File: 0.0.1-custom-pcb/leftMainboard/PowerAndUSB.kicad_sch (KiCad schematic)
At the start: 31 parts, among them J1 USB-C USB2 receptacle (footpr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, J2 3-pin LiPo / NTC 1.25mm (esti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, Q2 P-channel MOSFET (guess), Q3 P-channel MOSFET (guess), SW1 Latching DPDT power push swit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, U1 Boost controller MSOP8 (unide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, U2 TP4056-42-ESOP8, U3 PRTR5V0U2X

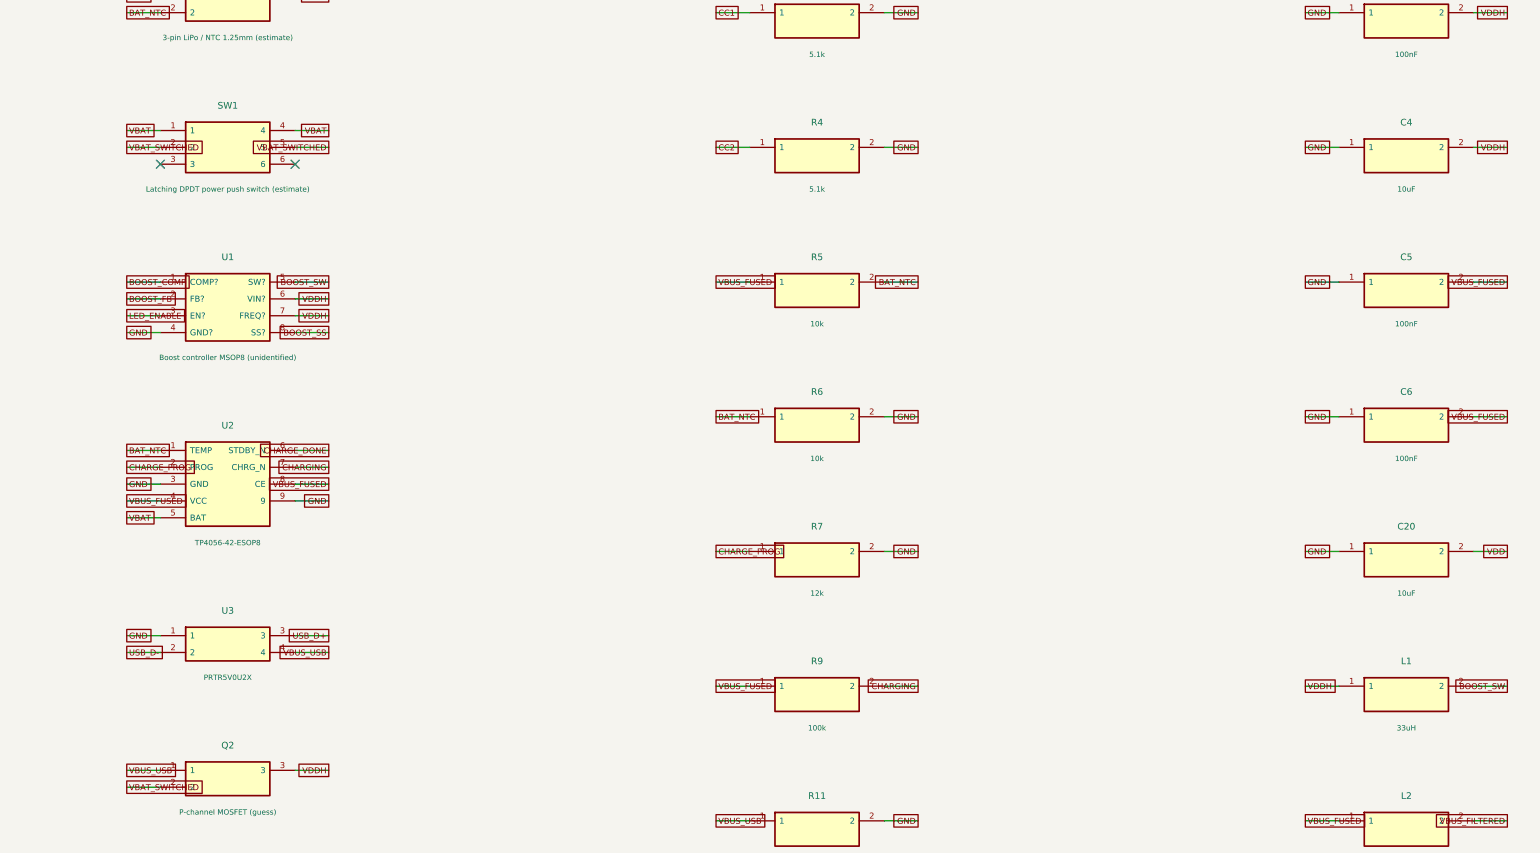
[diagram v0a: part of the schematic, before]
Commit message: get correct main switch
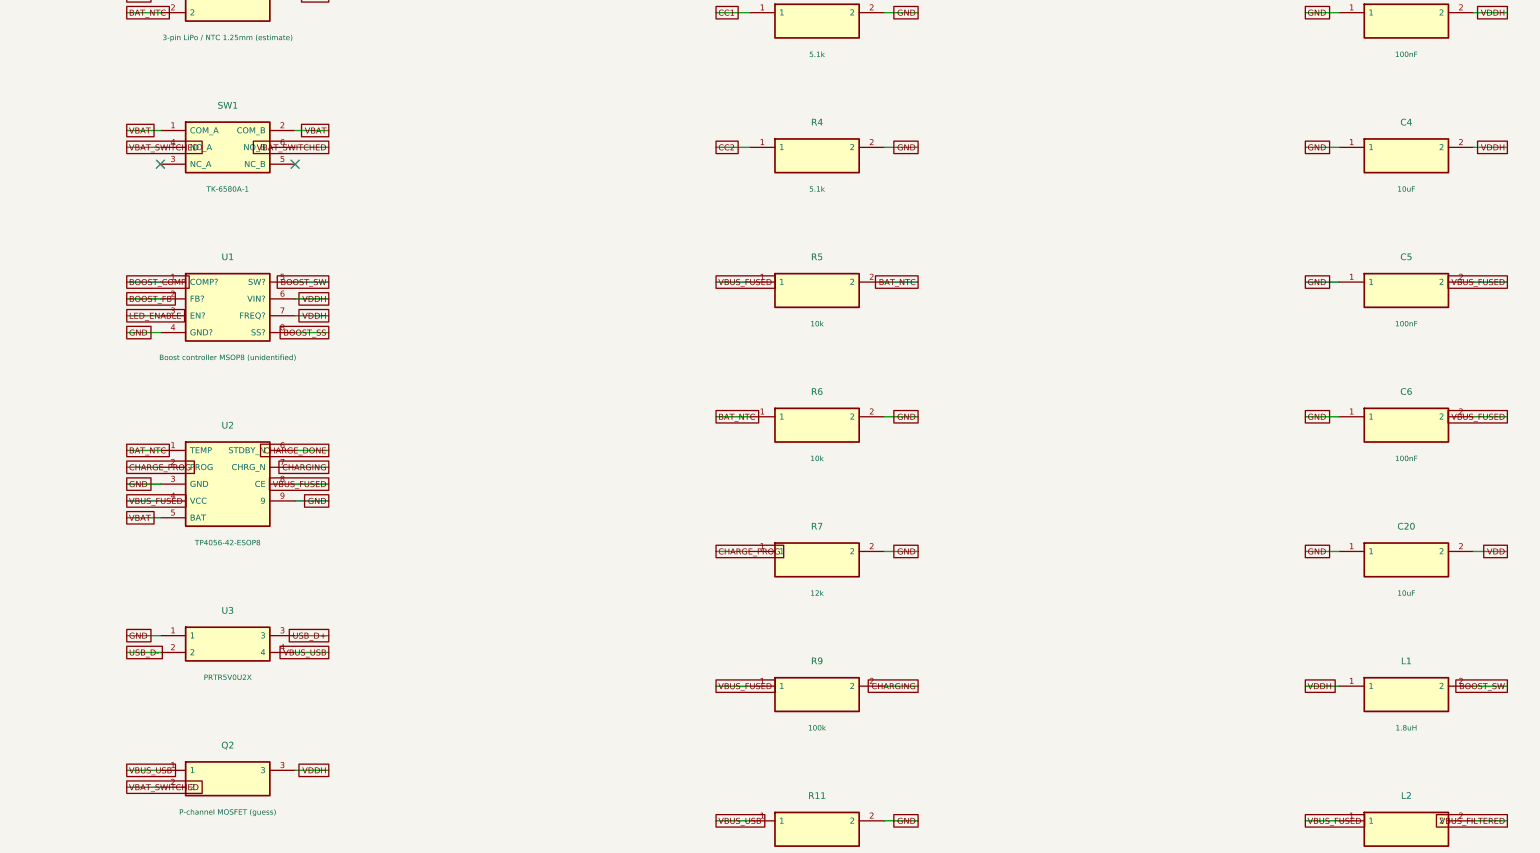
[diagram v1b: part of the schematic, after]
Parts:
- L1: value 33uH -> 1.8uH; footprint Reconstruction:L1_Inductor_6x6mm_PhotoEstimate -> Reconstruction:L_XRCD54_5.8x5.2mm_C5339378; symbol Reconstruction:L1_L1_Inductor_6x6mm_PhotoEstimate -> Reconstruction:L_XRCD54_1R8M_C5339378; Candidate part (none) -> XRCD54-1R8M; Confidence High (33uH marking) -> User-selected replacement; original part unconfirmed; Evidence L1 marked 330; L2/L3 values and exact function inferred -> C5339378 selected by user; supersedes photo-estimated 33uH; LCSC Part (none) -> C5339378; MPN (none) -> XRCD54-1R8M; Manufacturer (none) -> XR
- SW1: value Latching DPDT power push switch (estimate) -> TK-6580A-1; footprint Reconstruction:PowerSwitch_DPDT_LH_PhotoEstimate -> Reconstruction:SW_TK6580A1_C528770; symbol Reconstruction:SW1_PowerSwitch_DPDT_LH_PhotoEstimate -> Reconstruction:SW_TK6580A1_C528770; Candidate part PS-22F family, verify dimensional drawing -> TK-6580A-1; Confidence Low -> User-selected replacement; original part unconfirmed; Evidence Push actuator + six contacts + mechanical lugs visible; exa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 -> User-selected replacement; footprint and models from JLCEDA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; LCSC Part (none) -> C528770; MPN (none) -> TK-6580A-1; Manufacturer (none) -> Yuandi
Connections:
- net VBAT: now also SW1.2 (COM_B); no longer SW1.4
- net VBAT_SWITCHED: now also SW1.4 (NO_A), SW1.6 (NO_B); no longer SW1.2, SW1.5
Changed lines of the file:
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@@
 (no_connect (at 66.04 110.49)
 )
-(symbol (lib_id "Reconstruction:SW1_PowerSwitch_DPDT_LH_PhotoEstimate")
-(at 55.88 107.94999999999999 0)
-(unit 1)
-(exclude_from_sim no)
-(in_bom yes)
-(on_board yes)
-(dnp no)
-(property "Reference" "SW1" (at 55.88 101.63999999999999 0)
-(effects (font (size 1.0 1.0))))
-(property "Value" "Latching DPDT power push switch (estimate)" (at 55.88 114.25999999999999 0)
-(effects (font (size 0.8 0.8))))
-(property "Footprint" "Reconstruction:PowerSwitch_DPDT_LH_PhotoEstimate" (at 55.88 107.94999999999999 0)
-(effects (font (size 1.0 1.0))
-(hide yes)))
-(property "Datasheet" "" (at 55.88 107.94999999999999 0)
-(effects (font (size 1.0 1.0))
-(hide yes)))
-(property "Confidence" "Low" (at 55.88 107.94999999999999 0)
-(effects (font (size 1.0 1.0))
-(hide yes)))
-(property "Evidence" "Push actuator + six contacts + mechanical lugs visible; exact switch/terminal function unverified" (at 55.88 107.94999999999999 0)
-(effects (font (size 1.0 1.0))
-(hide yes)))
-(property "Candidate part" "PS-22F family, verify dimensional drawing" (at 55.88 107.94999999999999 0)
-(effects (font (size 1.0 1.0))
-(hide yes)))
-(pin "1")
-(pin "2")
-(pin "3")
-(pin "4")
-(pin "5")
-(pin "6")
-(instances (project "leftMainboard" (path "/eac6e0a1-0901-4c4d-b0b4-c941afc6d33b/3d4a4145-dfbf-4d53-839d-da2f670b524e" (reference "SW1")
-(unit 1)))))
+(symbol (lib_id "Reconstruction:SW_TK6580A1_C528770") (at 55.88 107.94999999999999 0) (unit 1) (exclude_from_sim no) (in_bom yes) (on_board yes) (dnp no) (property "Reference" "SW1" (at 55.88 101.63999999999999 0) (effects (font (size 1.0 1.0)))) (property "Value" "TK-6580A-1" (at 55.88 114.25999999999999 0) (effects (font (size 0.8 0.8)))) (property "Footprint" "Reconstruction:SW_TK6580A1_C528770" (at 55.88 107.94999999999999 0) (effects (font (size 1.0 1.0)) (hide yes))) (property "Datasheet" "https://wmsc.lcsc.com/wmsc/upload/file/pdf/v2/lcsc/2304140030_Yuandi-TK-6580A-1_C528770.pdf" (at 55.88 107.94999999999999 0) (effects (font (size 1.0 1.0)) (hide yes))) (property "Confidence" "User-selected replacement; original part unconfirmed" (at 55.88 107.94999999999999 0) (effects (font (size 1.0 1.0)) (hide yes))) (property "Evidence" "User-selected replacement; footprint and models from JLCEDA/EasyEDA Official Library; pin function checked against manufacturer drawing" (at 55.88 107.94999999999999 0) (effects (font (size 1.0 1.0)) (hide yes))) (property "Candidate part" "TK-6580A-1" (at 55.88 107.94999999999999 0) (effects (font (size 1.0 1.0)) (hide yes))) (pin "1") (pin "4") (pin "3") (pin "2") (pin "6") (pin "5") (instances (project "leftMainboard" (path "/eac6e0a1-0901-4c4d-b0b4-c941afc6d33b/3d4a4145-dfbf-4d53-839d-da2f670b524e" (reference "SW1") (unit 1)))) (property "LCSC Part" "C528770" (at 55.88 107.94999999999999 0) (effects (font (size 1.0 1.0)) (hide yes))) (property "Manufacturer" "Yuandi" (at 55.88 107.94999999999999 0) (effects (font (size 1.0 1.0)) (hide yes))) (property "MPN" "TK-6580A-1" (at 55.88 107.94999999999999 0) (effects (font (size 1.0 1.0)) (hide yes))))
 (wire (pts (xy 45.72 128.27)
 (xy 40.64 128.27))
@@
 (effects (font (size 1.0 1.0))
 (hide yes))))
-(symbol (lib_id "Reconstruction:L1_L1_Inductor_6x6mm_PhotoEstimate")
-(at 233.68 190.49999999999994 0)
-(unit 1)
-(exclude_from_sim no)
-(in_bom yes)
-(on_board yes)
-(dnp no)
-(property "Reference" "L1" (at 233.68 185.45999999999995 0)
-(effects (font (size 1.0 1.0))))
-(property "Value" "33uH" (at 233.68 195.53999999999994 0)
-(effects (font (size 0.8 0.8))))
-(property "Footprint" "Reconstruction:L1_Inductor_6x6mm_PhotoEstimate" (at 233.68 190.49999999999994 0)
-(effects (font (size 1.0 1.0))
-(hide yes)))
-(property "Datasheet" "" (at 233.68 190.49999999999994 0)
-(effects (font (size 1.0 1.0))
-(hide yes)))
-(property "Confidence" "High (33uH marking)" (at 233.68 190.49999999999994 0)
-(effects (font (size 1.0 1.0))
-(hide yes)))
-(property "Evidence" "L1 marked 330; L2/L3 values and exact function inferred" (at 233.68 190.49999999999994 0)
-(effects (font (size 1.0 1.0))
-(hide yes)))
-(property "Candidate part" "" (at 233.68 190.49999999999994 0)
-(effects (font (size 1.0 1.0))
-(hide yes)))
-(pin "1")
-(pin "2")
-(instances (project "leftMainboard" (path "/eac6e0a1-0901-4c4d-b0b4-c941afc6d33b/3d4a4145-dfbf-4d53-839d-da2f670b524e" (reference "L1")
-(unit 1)))))
+(symbol (lib_id "Reconstruction:L_XRCD54_1R8M_C5339378") (at 233.68 190.49999999999994 0) (unit 1) (exclude_from_sim no) (in_bom yes) (on_board yes) (dnp no) (property "Reference" "L1" (at 233.68 185.45999999999995 0) (effects (font (size 1.0 1.0)))) (property "Value" "1.8uH" (at 233.68 195.53999999999994 0) (effects (font (size 0.8 0.8)))) (property "Footprint" "Reconstruction:L_XRCD54_5.8x5.2mm_C5339378" (at 233.68 190.49999999999994 0) (effects (font (size 1.0 1.0)) (hide yes))) (property "Datasheet" "https://wmsc.lcsc.com/wmsc/upload/file/pdf/v2/lcsc/2212281609_XR-XRCD54-1R8M_C5339378.pdf" (at 233.68 190.49999999999994 0) (effects (font (size 1.0 1.0)) (hide yes))) (property "Confidence" "User-selected replacement; original part unconfirmed" (at 233.68 190.49999999999994 0) (effects (font (size 1.0 1.0)) (hide yes))) (property "Evidence" "C5339378 selected by user; supersedes photo-estimated 33uH" (at 233.68 190.49999999999994 0) (effects (font (size 1.0 1.0)) (hide yes))) (property "Candidate part" "XRCD54-1R8M" (at 233.68 190.49999999999994 0) (effects (font (size 1.0 1.0)) (hide yes))) (pin "1") (pin "2") (instances (project "leftMainboard" (path "/eac6e0a1-0901-4c4d-b0b4-c941afc6d33b/3d4a4145-dfbf-4d53-839d-da2f670b524e" (reference "L1") (unit 1)))) (property "LCSC Part" "C5339378" (at 233.68 190.49999999999994 0) (effects (font (size 1 1)) (hide yes))) (property "Manufacturer" "XR" (at 233.68 190.49999999999994 0) (effects (font (size 1 1)) (hide yes))) (property "MPN" "XRCD54-1R8M" (at 233.68 190.49999999999994 0) (effects (font (size 1 1)) (hide yes))))
 (wire (pts (xy 223.52 209.55)
 (xy 218.44 209.55))

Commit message: update a couple components to be correct
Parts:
- J2: value 3-pin LiPo / NTC 1.25mm (estimate) -> 53398-0371; footprint Reconstruction:Battery_3pin_1.25mm_PhotoEstimate -> Reconstruction:J_Molex_53398_0371_C293633; symbol Reconstruction:J2_Battery_3pin_1.25mm_PhotoEstimate -> Reconstruction:J_Molex_53398_0371_C293633; Candidate part JST GH / Molex PicoBlade 1.25mm family -> 53398-0371; Confidence Low (MPN and polarity) -> User-selected replacement; original part unconfirmed; Evidence 3-pin housing and three wires visible; pitch estimated from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 -> User-selected C293633 replacement; Molex PicoBlade 53398-03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; LCSC Part (none) -> C293633; MPN (none) -> 53398-0371; Manufacturer (none) -> Molex
- U1: value Boost controller MSOP8 (unidentified) -> SY7088DGC; footprint Reconstruction:U1_MSOP-8_3x3mm_P0.65mm -> Reconstruction:DFN8_SY7088DGC_2x3mm_C178240; symbol Reconstruction:U1_U1_MSOP-8_3x3mm_P0.65mm -> Reconstruction:U_SY7088DGC_C178240; Candidate part TPS61085-class MSOP8 boost; NOT confirmed pin-compatible -> SY7088DGC; Confidence Low -> High: marking and body size match; selected replacement; Evidence Marking looks MXCEA/M1CEA, unreadable ID. Guessed functiona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 -> User-reported VTGEA marking and approximately 2.1x3 mm body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; LCSC Part (none) -> C178240; MPN (none) -> SY7088DGC; Manufacturer (none) -> Silergy
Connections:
- net BOOST_COMP is gone; now on net BOOST_SW: U1.1 (LX)
- net BOOST_SS is gone; now on net VDD: U1.8 (OUT)
- net BOOST_FB: now also U1.5 (FB); no longer U1.2 (FB?)
- net BOOST_SW: now also U1.2 (LX); no longer U1.5 (SW?)
- net GND: now also J2.3 (GND), U1.9 (PGND); no longer J2.1
- net VBAT: now also J2.1 (VBAT); no longer J2.3
- net VDD: now also U1.7 (OUT)
- net VDDH: no longer U1.7 (FREQ?)

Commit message: update more of left main
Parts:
- F1: value 500mA resettable fuse (guess) -> MF-NSMF150-2; Confidence Medium (function), Low (rating) -> User selected; Evidence Gold B-marked rectangular part is likely PPTC USB protection -> Selected by user from the 8 marking and measured 3.4 x 1.8 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; LCSC (none) -> C89655; LCSC Part (none) -> C89655; MPN (none) -> MF-NSMF150-2; Manufacturer (none) -> Bourns
- Q3: value P-channel MOSFET (guess) -> BSS138 N-channel; Candidate part AO3401A / SI2301 family -> BSS138; Confidence Low -> Medium; Evidence 3-lead packages; faint SS/G marking; polarity and part numb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 -> User measured body about 3x1.3 mm, marking SS; diode-mode d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; LCSC (none) -> C7420339
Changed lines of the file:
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@@
 (property "Reference" "Q3" (at 55.88 218.47999999999996 0)
 (effects (font (size 1.0 1.0))))
-(property "Value" "P-channel MOSFET (guess)" (at 55.88 228.55999999999995 0)
+(property "Value" "BSS138 N-channel" (at 55.88 228.55999999999995 0)
 (effects (font (size 0.8 0.8))))
 (property "Footprint" "Reconstruction:Q3_SOT-23" (at 55.88 223.51999999999995 0)
 (effects (font (size 1.0 1.0))
 (hide yes)))
-(property "Datasheet" "" (at 55.88 223.51999999999995 0)
-(effects (font (size 1.0 1.0))
-(hide yes)))
-(property "Confidence" "Low" (at 55.88 223.51999999999995 0)
-(effects (font (size 1.0 1.0))
-(hide yes)))
-(property "Evidence" "3-lead packages; faint SS/G marking; polarity and part number unconfirmed" (at 55.88 223.51999999999995 0)
-(effects (font (size 1.0 1.0))
-(hide yes)))
-(property "Candidate part" "AO3401A / SI2301 family" (at 55.88 223.51999999999995 0)
+(property "Datasheet" "https://www.lcsc.com/datasheet/C7420339.pdf" (at 55.88 223.51999999999995 0)
+(effects (font (size 1.0 1.0))
+(hide yes)))
+(property "LCSC" "C7420339" (at 55.88 223.51999999999995 0)
+(effects (font (size 1.0 1.0))
+(hide yes)))
+(property "Confidence" "Medium" (at 55.88 223.51999999999995 0)
+(effects (font (size 1.0 1.0))
+(hide yes)))
+(property "Evidence" "User measured body about 3x1.3 mm, marking SS; diode-mode display 440 (about 0.440 V), pins 1/2 shorted, red 2 black 3; supports N-channel; reverse reading and isolated-device test not reported; exact MPN unconfirmed" (at 55.88 223.51999999999995 0)
+(effects (font (size 1.0 1.0))
+(hide yes)))
+(property "Candidate part" "BSS138" (at 55.88 223.51999999999995 0)
 (effects (font (size 1.0 1.0))
 (hide yes)))
@@
 (property "Reference" "F1" (at 322.58000000000004 83.85999999999999 0)
 (effects (font (size 1.0 1.0))))
-(property "Value" "500mA resettable fuse (guess)" (at 322.58000000000004 93.94 0)
+(property "Value" "MF-NSMF150-2" (at 322.58000000000004 93.94 0)
 (effects (font (size 0.8 0.8))))
 (property "Footprint" "Reconstruction:F1_Fuse_1206_3216Metric" (at 322.58000000000004 88.89999999999999 0)
 (effects (font (size 1.0 1.0))
 (hide yes)))
-(property "Datasheet" "" (at 322.58000000000004 88.89999999999999 0)
-(effects (font (size 1.0 1.0))
-(hide yes)))
-(property "Confidence" "Medium (function), Low (rating)" (at 322.58000000000004 88.89999999999999 0)
-(effects (font (size 1.0 1.0))
-(hide yes)))
-(property "Evidence" "Gold B-marked rectangular part is likely PPTC USB protection" (at 322.58000000000004 88.89999999999999 0)
-(effects (font (size 1.0 1.0))
-(hide yes)))
-(property "Candidate part" "" (at 322.58000000000004 88.89999999999999 0)
+(property "Datasheet" "https://www.bourns.com/docs/product-datasheets/mf-nsmf.pdf" (at 322.58000000000004 88.89999999999999 0)
+(effects (font (size 1.0 1.0))
+(hide yes)))
+(property "Confidence" "User selected" (at 322.58000000000004 88.89999999999999 0)
+(effects (font (size 1.0 1.0))
+(hide yes)))
+(property "Evidence" "Selected by user from the 8 marking and measured 3.4 x 1.8 mm package" (at 322.58000000000004 88.89999999999999 0)
+(effects (font (size 1.0 1.0))
+(hide yes)))
+(property "MPN" "MF-NSMF150-2" (at 322.58000000000004 88.89999999999999 0)
 (effects (font (size 1.0 1.0))
 (hide yes)))
@@
 (pin "2")
 (instances (project "leftMainboard" (path "/eac6e0a1-0901-4c4d-b0b4-c941afc6d33b/3d4a4145-dfbf-4d53-839d-da2f670b524e" (reference "F1")
-(unit 1)))))
+(unit 1))))
+(property "Description" "Bourns MF-NSMF150-2 resettable PPTC fuse; 1.5A hold, 3A trip, 6V; 1206 package; marking 8" (at 0 0 0) (effects (font (size 1 1)) (hide yes)))
+(property "Manufacturer" "Bourns" (at 0 0 0) (effects (font (size 1 1)) (hide yes)))
+(property "LCSC" "C89655" (at 0 0 0) (effects (font (size 1 1)) (hide yes)))
+(property "LCSC Part" "C89655" (at 0 0 0) (effects (font (size 1 1)) (hide yes)))
+)
 (text "CONFIRMED: GPIO and SWD mappings from MoErgo documentation and ZMK.\nINFERRED: component values, power circuitry, battery polarity and replacement MPNs.\nAll pins of unidentified ICs are passive for evidence capture; ERC cannot establish circuit correctness." (at 20 15 0)
 (effects (font (size 1.0 1.0))
